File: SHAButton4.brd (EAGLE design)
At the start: 40 x 45 mm, 5 parts, among them SW1 SWITCH-SPDT-ILLUMINATED, SW2 SWITCH-SPDT-ILLUMINATED, SW3 SWITCH-SPDT-ILLUMINATED, SW4 SWITCH-SPDT-ILLUMINATED

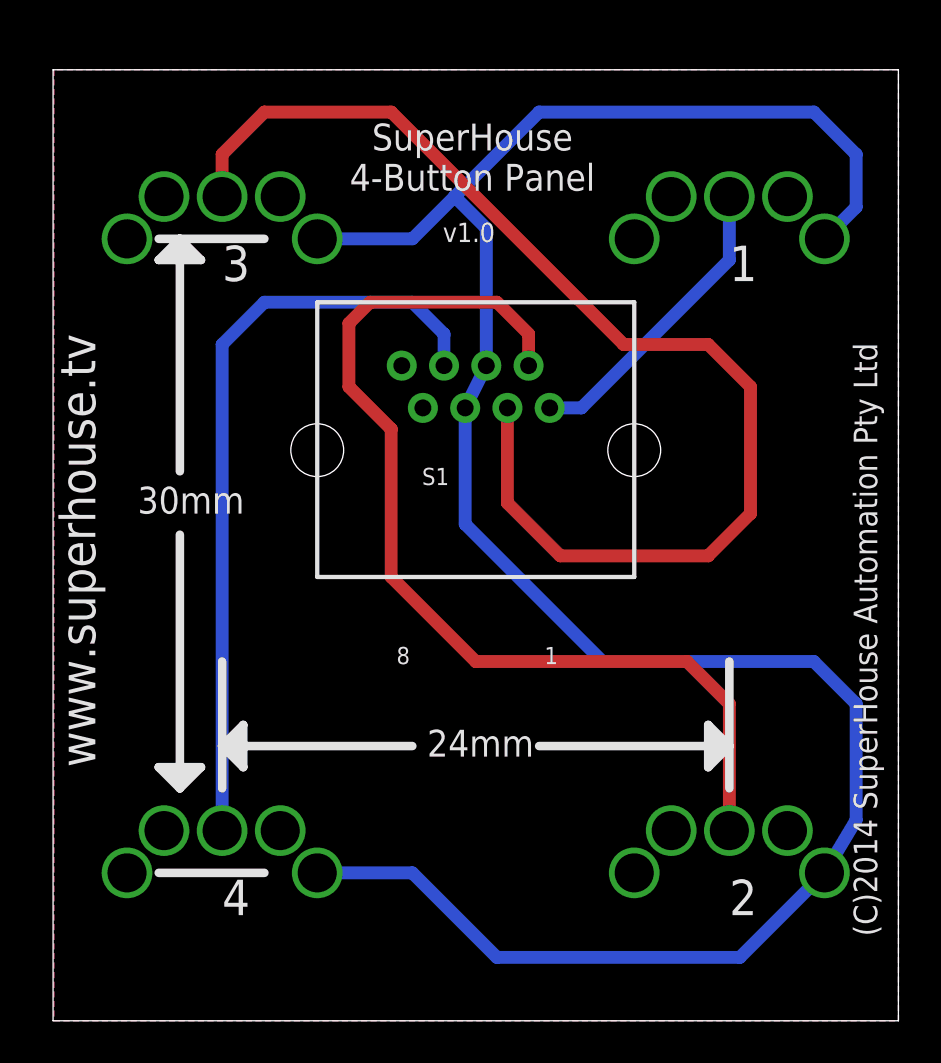
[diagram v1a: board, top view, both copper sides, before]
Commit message: Replaced buttons with more common SPST type
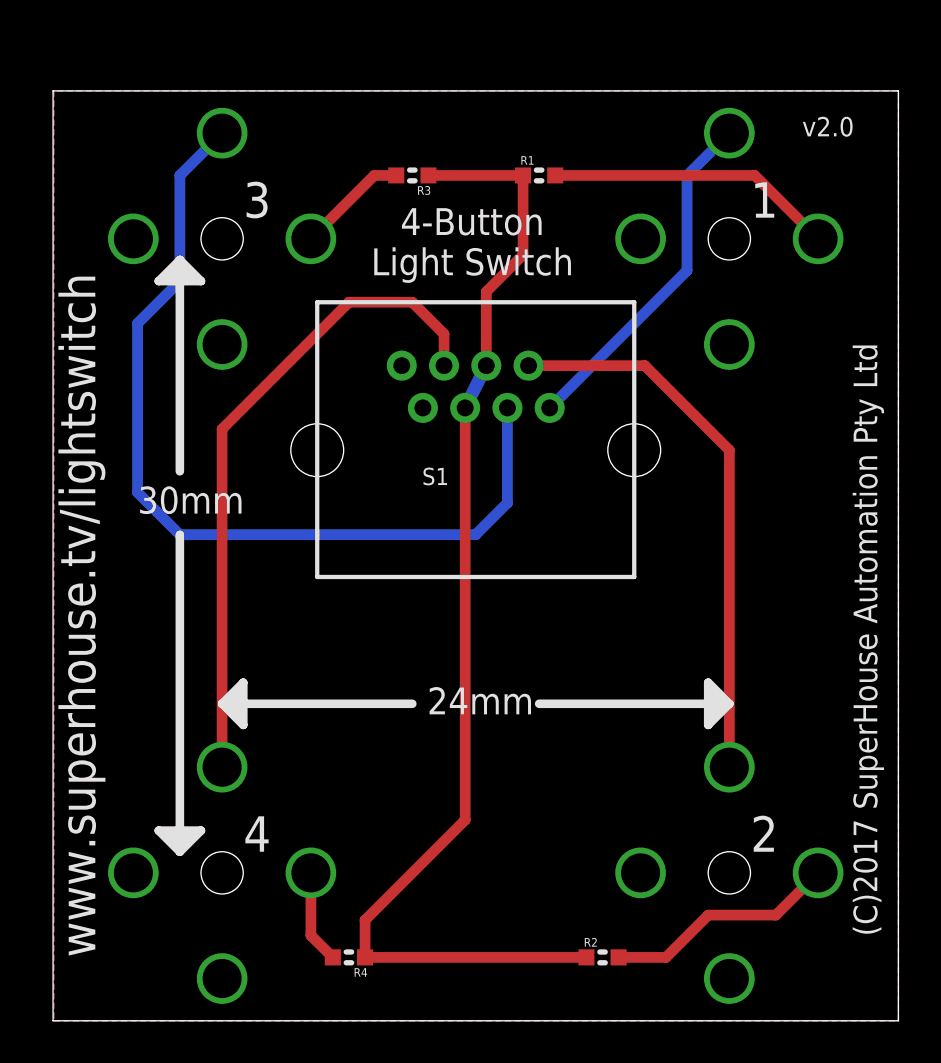
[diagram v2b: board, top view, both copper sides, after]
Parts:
- added R1, R2, R3, R4: 3K3, freetronics-jon:0603
- SW1, SW2, SW3, SW4: value SWITCH-SPDT-ILLUMINATED -> SWITCH-SPST-ILLUMINATED; device freetronics-jon:SWITCH-SPDT-ILLUMINATED -> freetronics-jon:SWITCH-SPST-ILLUMINATED
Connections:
- new net N$1: R2.2, SW2.2
- new net N$6: R1.2, SW1.2
- new net N$7: R3.2, SW3.2
- new net N$8: R4.2, SW4.2
- net +12V: now also R1.1, R2.1, R3.1, R4.1; no longer SW1.1, SW2.1, SW3.1, SW4.1
- net GND: now also SW1.1, SW1.4, SW2.1, SW2.4, SW3.1, SW3.4, SW4.1, SW4.4; no longer SW1.2, SW1.5, SW2.2, SW2.5, SW3.2, SW3.5, SW4.2, SW4.5
- net N$2: now also SW3.3; no longer SW3.4
- net N$3: now also SW4.3; no longer SW4.4
- net N$4: now also SW1.3; no longer SW1.4
- net N$5: now also SW2.3; no longer SW2.4
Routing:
- net +12V: track 107.5 -> 54.9 mm
- net N$5: track 48.3 -> 26.2 mm
- net N$2: track 57.1 -> 42.1 mm
- net N$6: track 0.00 -> 13.7 mm
- net N$1: track 0.00 -> 11.1 mm
- net N$3: track 36.4 -> 31.1 mm
- net N$7: track 0.00 -> 5.28 mm
- net N$8: track 0.00 -> 4.43 mm
- net N$4: track 14.4 -> 16.5 mm
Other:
- board size 40 x 45 mm -> 40 x 44 mm
- board text added: "(C)2017 SuperHouse Automation Pty Ltd"
- board text added: "4-Button Light Switch"
- board text added: "v2.0"
- board text added: "www.superhouse.tv/lightswitch"
- board text removed: "(C)2014 SuperHouse Automation Pty Ltd"
- board text removed: "8"
- board text removed: "SuperHouse 4-Button Panel"
- board text removed: "v1.0"
- board text removed: "www.superhouse.tv"

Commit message: Replaced buttons
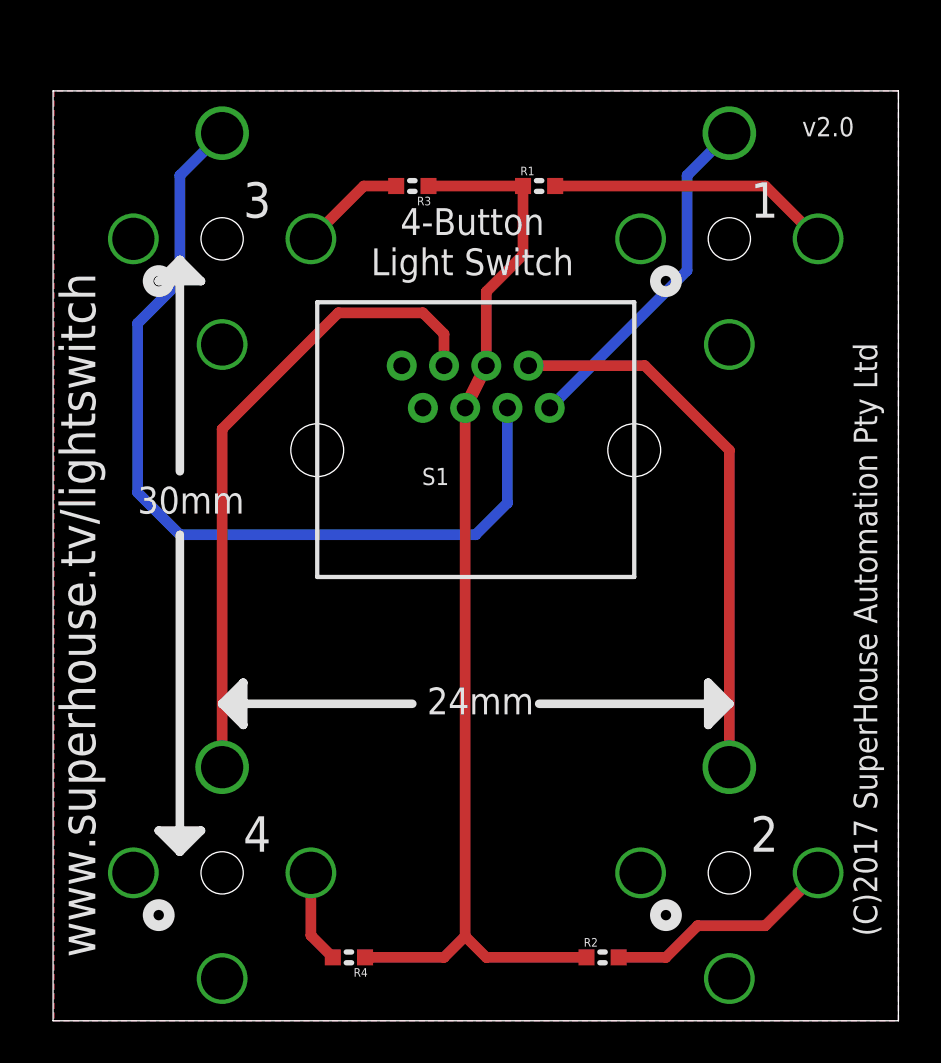
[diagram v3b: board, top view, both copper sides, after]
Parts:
- moved R1 0.50 mm to (23.0, 39.5)
- moved R3 0.50 mm to (17.0, 39.5)
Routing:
- net +12V: track 54.9 -> 52.2 mm
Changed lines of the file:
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@@
 <setting verticaltext="up"/>
 </settings>
-<grid distance="1" unitdist="mm" unit="mm" style="dots" multiple="1" display="yes" altdistance="0.001" altunitdist="inch" altunit="inch"/>
+<grid distance="0.5" unitdist="mm" unit="mm" style="dots" multiple="1" display="yes" altdistance="0.001" altunitdist="inch" altunit="inch"/>
 <layers>
 <layer number="1" name="Top" color="4" fill="1" visible="yes" active="yes"/>
@@
 <hole x="32" y="37" drill="2"/>
 <hole x="8" y="37" drill="2"/>
+<circle x="29" y="35" radius="0.5" width="0.508" layer="21"/>
+<circle x="29" y="5" radius="0.5" width="0.508" layer="21"/>
+<circle x="5" y="5" radius="0.5" width="0.508" layer="21"/>
+<circle x="5" y="35" radius="0.5" width="0.508" layer="21"/>
 </plain>
 <attributes>
@@
 <element name="SW3" library="freetronics-jon" package="SWITCH-SPST-ILLUMINATED" value="SWITCH-SPST-ILLUMINATED" x="8" y="37" rot="MR0"/>
 <element name="SW4" library="freetronics-jon" package="SWITCH-SPST-ILLUMINATED" value="SWITCH-SPST-ILLUMINATED" x="8" y="7" rot="MR0"/>
-<element name="R1" library="freetronics-jon" package="0603" value="3K3" x="23" y="40"/>
+<element name="R1" library="freetronics-jon" package="0603" value="3K3" x="23" y="39.5"/>
 <element name="R2" library="freetronics-jon" package="0603" value="3K3" x="26" y="3"/>
-<element name="R3" library="freetronics-jon" package="0603" value="3K3" x="17" y="40" rot="R180"/>
+<element name="R3" library="freetronics-jon" package="0603" value="3K3" x="17" y="39.5" rot="R180"/>
 <element name="R4" library="freetronics-jon" package="0603" value="3K3" x="14" y="3" rot="R180"/>
 </elements>
@@
 <contactref element="S1" pad="5"/>
 <contactref element="S1" pad="4"/>
-<wire x1="19.5" y1="29" x2="20.5" y2="31" width="0.6096" layer="16"/>
+<wire x1="19.5" y1="29" x2="20.5" y2="31" width="0.6096" layer="1"/>
 <contactref element="R4" pad="1"/>
 <contactref element="R3" pad="1"/>
 <contactref element="R2" pad="1"/>
 <contactref element="R1" pad="1"/>
-<wire x1="22.238" y1="40" x2="17.762" y2="40" width="0.508" layer="1"/>
+<wire x1="22.238" y1="39.5" x2="17.762" y2="39.5" width="0.508" layer="1"/>
 <wire x1="20.5" y1="31" x2="20.5" y2="34.5" width="0.508" layer="1"/>
-<wire x1="22.238" y1="36.238" x2="22.238" y2="40" width="0.508" layer="1"/>
+<wire x1="22.238" y1="36.238" x2="22.238" y2="39.5" width="0.508" layer="1"/>
 <wire x1="20.5" y1="34.5" x2="22.238" y2="36.238" width="0.508" layer="1"/>
-<wire x1="19.5" y1="29" x2="19.5" y2="9.5" width="0.508" layer="1"/>
-<wire x1="14.762" y1="3" x2="14.762" y2="4.762" width="0.508" layer="1"/>
-<wire x1="19.5" y1="9.5" x2="14.762" y2="4.762" width="0.508" layer="1"/>
-<wire x1="25.238" y1="3" x2="14.762" y2="3" width="0.508" layer="1"/>
+<wire x1="19.5" y1="4" x2="20.5" y2="3" width="0.508" layer="1"/>
+<wire x1="20.5" y1="3" x2="25.238" y2="3" width="0.508" layer="1"/>
+<wire x1="19.5" y1="29" x2="19.5" y2="4" width="0.508" layer="1"/>
+<wire x1="14.762" y1="3" x2="18.5" y2="3" width="0.508" layer="1"/>
+<wire x1="18.5" y1="3" x2="19.5" y2="4" width="0.508" layer="1"/>
 </signal>
 <signal name="N$4">
@@
 <contactref element="SW4" pad="3"/>
 <wire x1="8" y1="12" x2="8" y2="28" width="0.508" layer="1"/>
-<wire x1="8" y1="28" x2="14" y2="34" width="0.508" layer="1"/>
-<wire x1="14" y1="34" x2="17" y2="34" width="0.508" layer="1"/>
-<wire x1="17" y1="34" x2="18.5" y2="32.5" width="0.508" layer="1"/>
+<wire x1="8" y1="28" x2="13.5" y2="33.5" width="0.508" layer="1"/>
+<wire x1="13.5" y1="33.5" x2="17.5" y2="33.5" width="0.508" layer="1"/>
+<wire x1="17.5" y1="33.5" x2="18.5" y2="32.5" width="0.508" layer="1"/>
 <wire x1="18.5" y1="32.5" x2="18.5" y2="31" width="0.508" layer="1"/>
 </signal>
@@
 <contactref element="SW2" pad="2"/>
 <contactref element="R2" pad="2"/>
-<wire x1="29" y1="3" x2="31" y2="5" width="0.508" layer="1"/>
-<wire x1="34.2" y1="5" x2="36.2" y2="7" width="0.508" layer="1"/>
+<wire x1="29" y1="3" x2="30.5" y2="4.5" width="0.508" layer="1"/>
+<wire x1="33.7" y1="4.5" x2="36.2" y2="7" width="0.508" layer="1"/>
 <wire x1="26.762" y1="3" x2="29" y2="3" width="0.508" layer="1"/>
-<wire x1="31" y1="5" x2="34.2" y2="5" width="0.508" layer="1"/>
+<wire x1="30.5" y1="4.5" x2="33.7" y2="4.5" width="0.508" layer="1"/>
 </signal>
 <signal name="N$6">
 <contactref element="SW1" pad="2"/>
 <contactref element="R1" pad="2"/>
-<wire x1="23.762" y1="40" x2="33.2" y2="40" width="0.508" layer="1"/>
-<wire x1="33.2" y1="40" x2="36.2" y2="37" width="0.508" layer="1"/>
+<wire x1="23.762" y1="39.5" x2="33.7" y2="39.5" width="0.508" layer="1"/>
+<wire x1="33.7" y1="39.5" x2="36.2" y2="37" width="0.508" layer="1"/>
 </signal>
 <signal name="N$7">
 <contactref element="SW3" pad="2"/>
 <contactref element="R3" pad="2"/>
-<wire x1="16.238" y1="40" x2="15.2" y2="40" width="0.508" layer="1"/>
-<wire x1="15.2" y1="40" x2="12.2" y2="37" width="0.508" layer="1"/>
+<wire x1="16.238" y1="39.5" x2="14.7" y2="39.5" width="0.508" layer="1"/>
+<wire x1="14.7" y1="39.5" x2="12.2" y2="37" width="0.508" layer="1"/>
 </signal>
 <signal name="N$8">
